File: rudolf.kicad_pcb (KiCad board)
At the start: 2 copper layers, 39.8 x 54.8 mm, 38 parts, among them J1 Conn_2Rows-05Pins, Q1 AO3401A, Q2 AO3401A, Q3 AO3401A, SW1 SW_DPST_x2, U1 PY32F002AF15P6TU

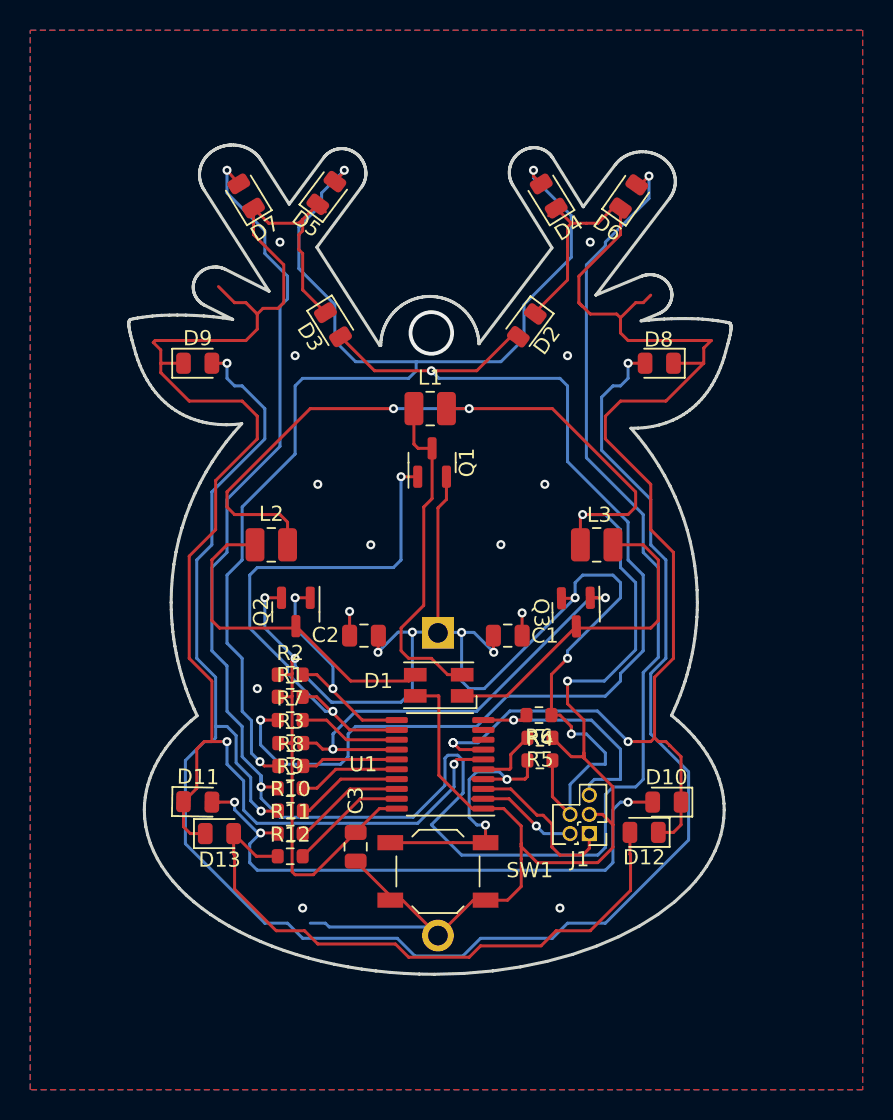
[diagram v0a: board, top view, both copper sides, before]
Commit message: Add revB
Fixed several issues where traces were unnecessarily complicated or at 90-degree angles. 
Most of these were corrected, especially on the bottom layer, except where the design intentionally required them. 
-Added component names to the silkscreen layer. 
-Moved the battery holder slightly upward as it was hanging off the bottom.
-Added the revision number on the back side.
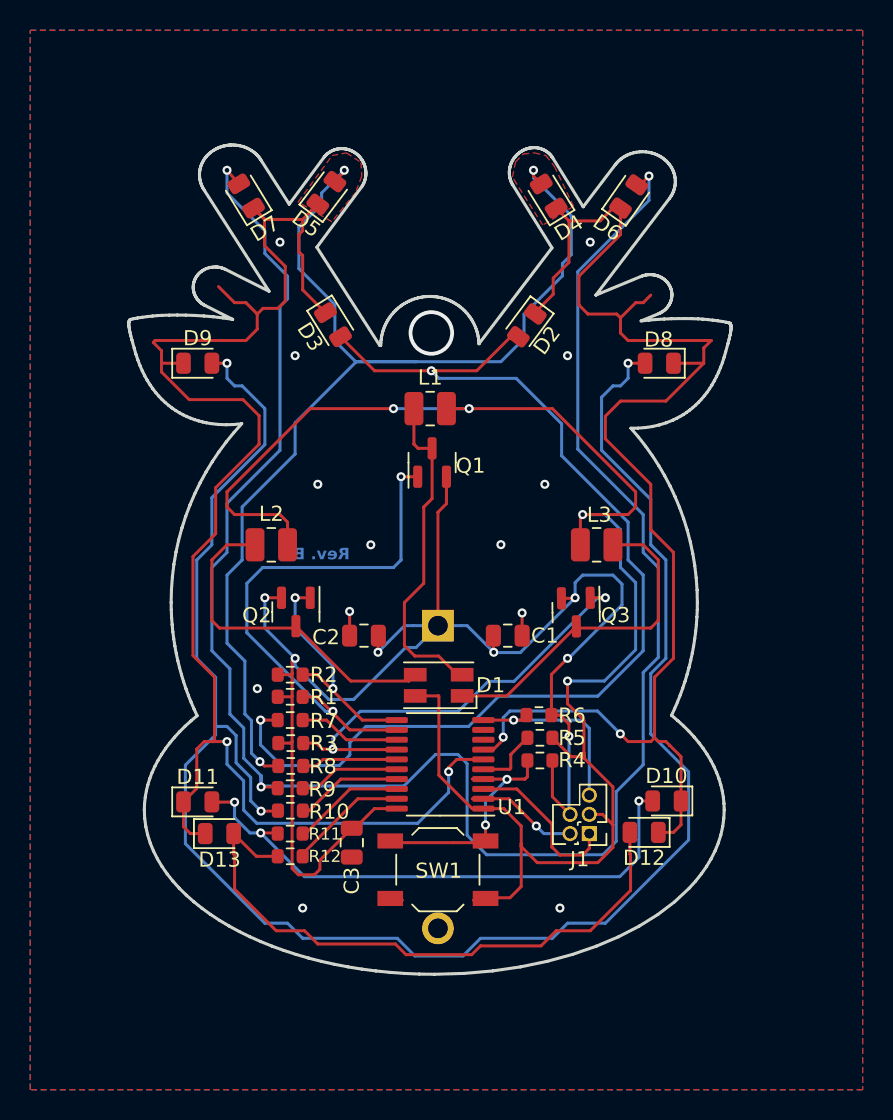
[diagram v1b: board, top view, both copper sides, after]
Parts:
- moved BT1 0.48 mm to (157.5, 81.3)
- moved C3 0.37 mm to (151.8, 95.6)
- moved SW1 0.12 mm to (157.5, 97.4)
- moved D10 0.08 mm to (172.6, 92.8)
- turned D11 to 0 degrees
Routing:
- net GND: track 131.7 -> 113.9 mm
- net VCC: track 113.0 -> 103.0 mm, vias 9 -> 7
- net Net-(D6-A): track 135.1 -> 129.0 mm
- net /MPX2: track 95.5 -> 91.2 mm, vias 3 -> 2
- net /nRST: track 15.9 -> 12.8 mm
- net Net-(SW1A-A): track 19.1 -> 15.9 mm
- net Net-(D2-A): track 74.9 -> 72.6 mm
- net Net-(D4-A): track 80.6 -> 78.8 mm
- net Net-(D10-A): track 38.5 -> 37.2 mm
- net /MPX1: track 102.5 -> 101.9 mm
- net Net-(D1-BK): track 22.6 -> 22.1 mm
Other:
- board text added: "Rev. B"
